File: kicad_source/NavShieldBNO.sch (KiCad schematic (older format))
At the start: 40 parts, among them CN1 ARDUINO_MKR, CN2 CONN_01X04, CN3 CONN_01X04, U1 BNO085, U2 BMP388

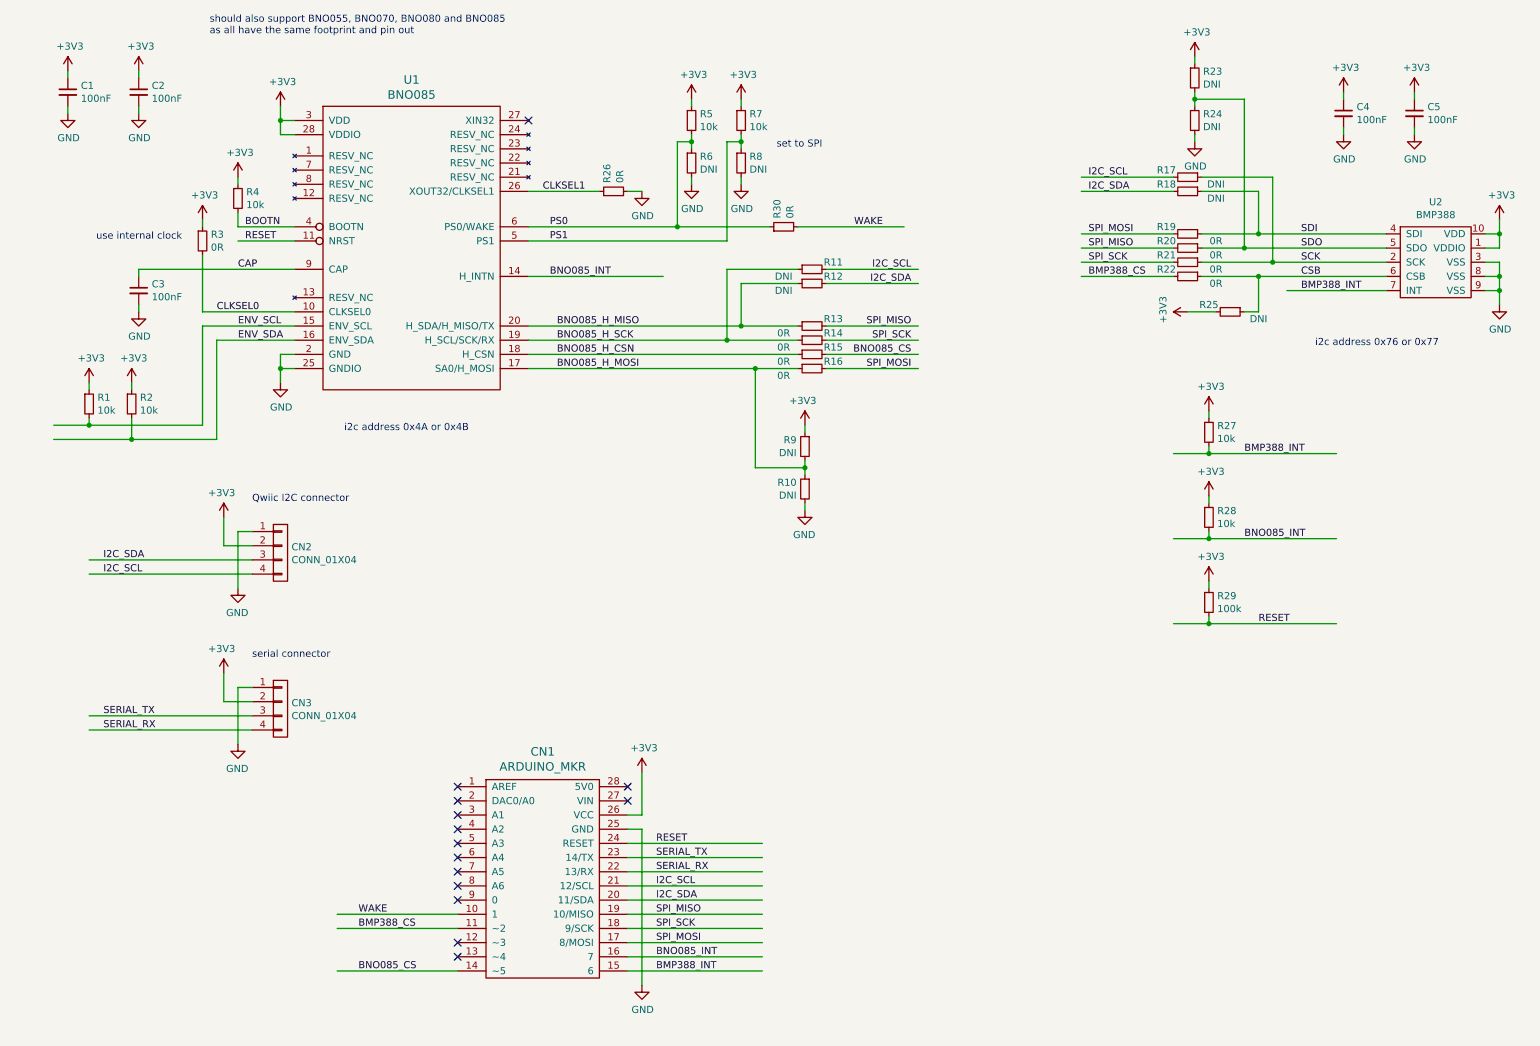
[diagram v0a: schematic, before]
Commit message: added second option for wake on A5, rearranged placement of option resistors and added description in silk screen
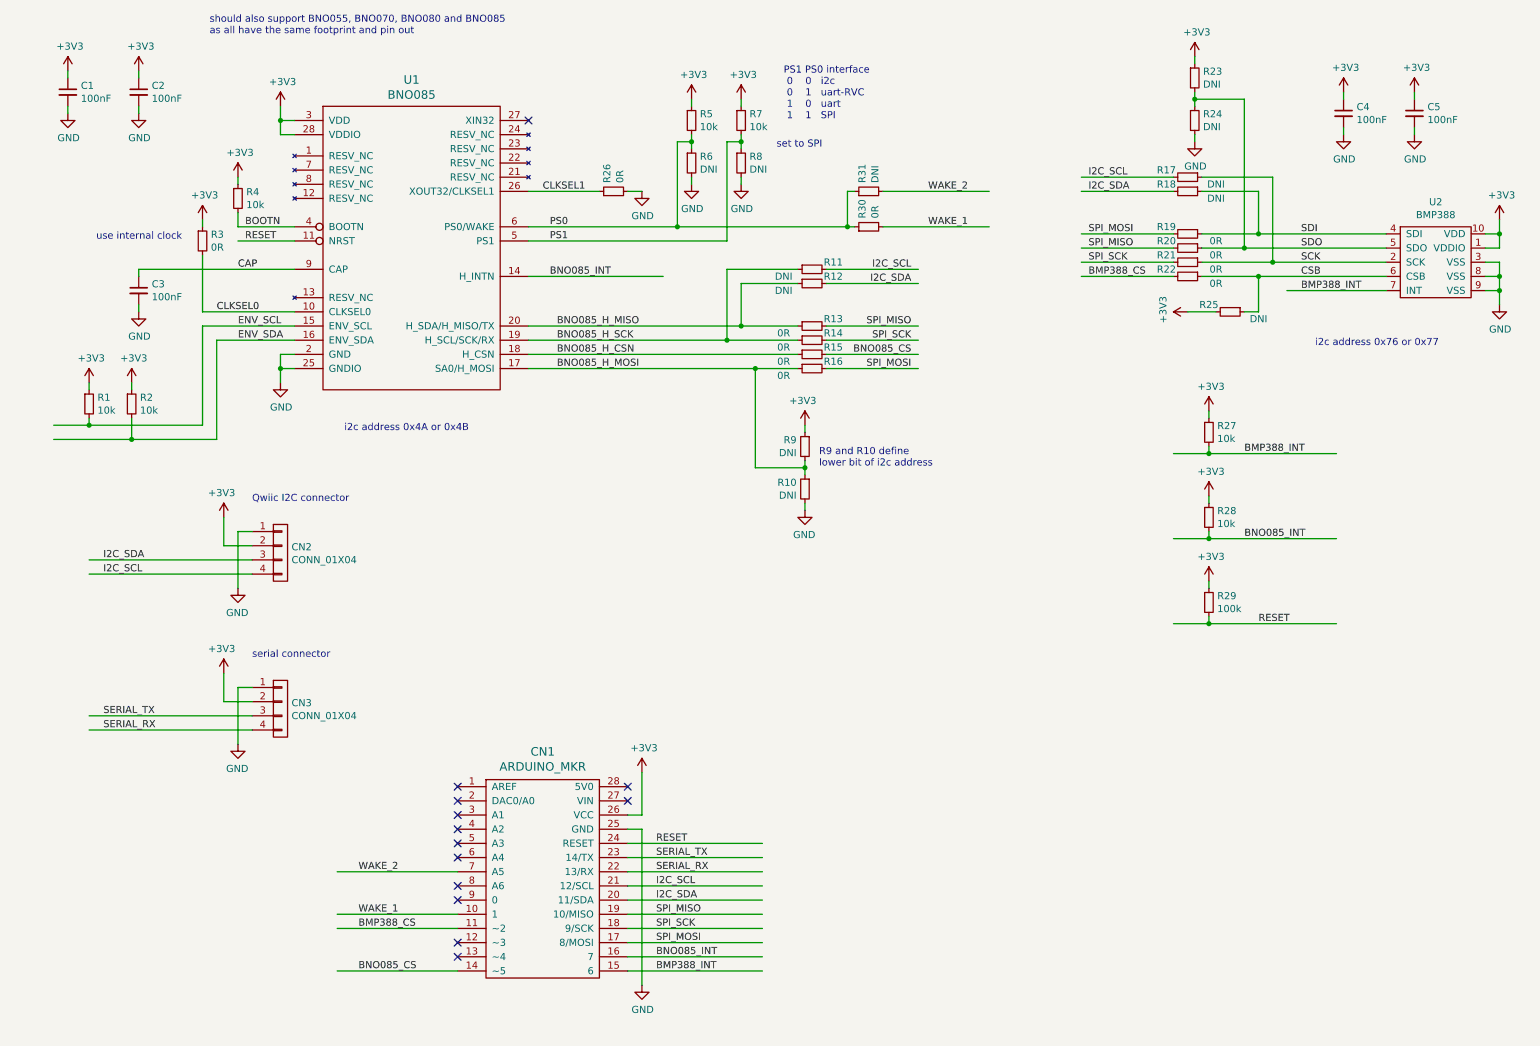
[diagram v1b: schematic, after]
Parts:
- added R31: DNI, resistors:R_0603, symbol devices:R_0603
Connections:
- net labels added: WAKE_1, WAKE_2
- net labels removed: WAKE
- wire segments 159 -> 164
- no-connect marks 14 -> 13
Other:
- note added: "PS1 PS0 interface\n 0 0 i2c\n 0 1 uart-RVC\n 1 0 uart\n 1 1 SPI\n"
- note added: "R9 and R10 define \nlower bit of i2c address"
- moved on the sheet: R30
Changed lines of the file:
@@
 Sheet 1 1
 Title "NavShieldBNO"
-Date "2020-09-17"
+Date "2020-09-25"
 Rev "dev_0.1"
 Comp "generationmake"
@@
 NoConn ~ 3650 6800
 NoConn ~ 3650 6700
-NoConn ~ 3650 6600
 NoConn ~ 3650 6500
 NoConn ~ 3650 6400
@@
 L devices:R_0603 R30
 U 1 1 5F6453B8
-P 5950 2050
-F 0 "R30" H 6009 2096 50  0000 L CNN
-F 1 "0R" H 6009 2005 50  0000 L CNN
-F 2 "resistors:R_0603" H 5950 1900 50  0001 C CNN
-F 3 "" H 5950 2050 50  0000 C CNN
-	1    5950 2050
+P 6550 2050
+F 0 "R30" H 6609 2096 50  0000 L CNN
+F 1 "0R" H 6609 2005 50  0000 L CNN
+F 2 "resistors:R_0603" H 6550 1900 50  0001 C CNN
+F 3 "" H 6550 2050 50  0000 C CNN
+	1    6550 2050
 	0    -1   -1   0
 $EndComp
 Wire Wire Line
-	6800 2050 6050 2050
-Wire Wire Line
-	5850 2050 5200 2050
-Connection ~ 5200 2050
-Text Label 6650 2050 2    50   ~ 0
-WAKE
+	7400 2050 6650 2050
+Wire Wire Line
+	6450 2050 6400 2050
+Text Label 7250 2050 2    50   ~ 0
+WAKE_1
 Wire Wire Line
 	2800 6900 3650 6900
 Text Label 2950 6900 0    50   ~ 0
-WAKE
+WAKE_1
 $Comp
 L mechanical-connectors:CONN_01X04 CN2
@@
 Text Label 4350 2750 0    50   ~ 0
 BNO085_H_MISO
+$Comp
+L devices:R_0603 R31
+U 1 1 5F6DCF1C
+P 6550 1800
+F 0 "R31" H 6609 1846 50  0000 L CNN
+F 1 "DNI" H 6609 1755 50  0000 L CNN
+F 2 "resistors:R_0603" H 6550 1650 50  0001 C CNN
+F 3 "" H 6550 1800 50  0000 C CNN
+	1    6550 1800
+	0    -1   -1   0
+$EndComp
+Text Label 7250 1800 2    50   ~ 0
+WAKE_2
+Wire Wire Line
+	7400 1800 6650 1800
+Wire Wire Line
+	6450 1800 6400 1800
+Wire Wire Line
+	6400 1800 6400 2050
+Connection ~ 6400 2050
+Wire Wire Line
+	2800 6600 3650 6600
+Text Label 2950 6600 0    50   ~ 0
+WAKE_2
+Wire Wire Line
+	5200 2050 6400 2050
+Connection ~ 5200 2050
+Text Notes 6200 3750 0    50   ~ 0
+R9 and R10 define \nlower bit of i2c address
+Text Notes 5950 1300 0    50   ~ 0
+PS1 PS0 interface\n 0    0   i2c\n 0    1   uart-RVC\n 1    0   uart\n 1    1   SPI\n
 $EndSCHEMATC

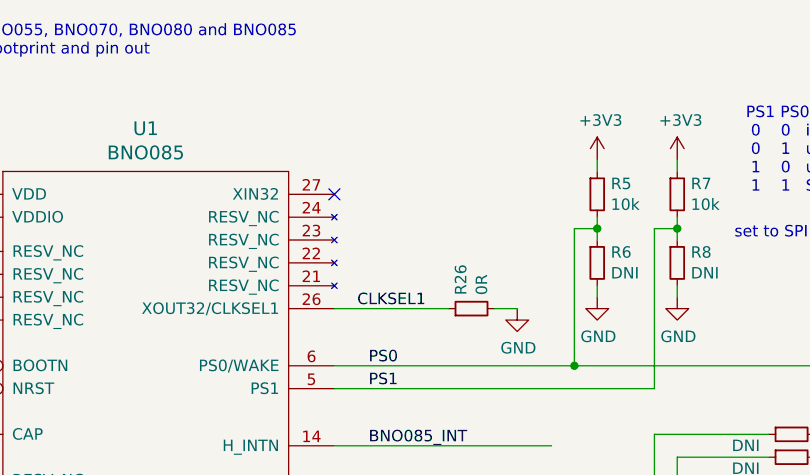
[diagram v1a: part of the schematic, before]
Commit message: added option for 32 kHz crystal, updated images and pdf
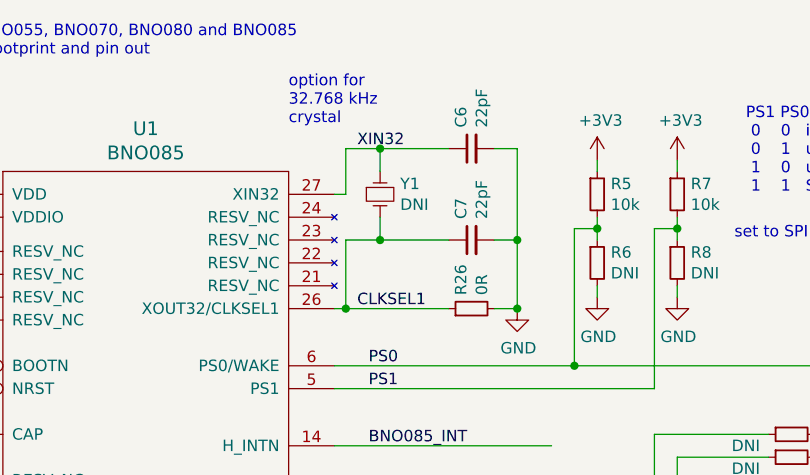
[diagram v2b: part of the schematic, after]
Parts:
- added C6, C7: 22pF, capacitors:C_0603, symbol devices:C_0603
- added Y1: DNI, crystals:Crystal_SMD_3.2x1.5mm_2Pad, symbol devices:Crystal_Small
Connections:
- net labels added: XIN32
- wire segments 164 -> 178
- no-connect marks 13 -> 12
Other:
- note added: "option for\n32.768 kHz\ncrystal"
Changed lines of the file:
@@
 Text Label 2950 7300 0    50   ~ 0
 BNO085_CS
-NoConn ~ 4150 1300
 Wire Wire Line
 	1400 2350 2500 2350
@@
 $EndComp
 Wire Wire Line
-	4150 1800 4650 1800
+	4150 1800 4200 1800
 Wire Wire Line
 	4850 1800 4950 1800
@@
 Text Notes 5950 1300 0    50   ~ 0
 PS1 PS0 interface\n 0    0   i2c\n 0    1   uart-RVC\n 1    0   uart\n 1    1   SPI\n
+$Comp
+L devices:Crystal_Small Y1
+U 1 1 5F6DCF85
+P 4350 1300
+F 0 "Y1" V 4304 1388 50  0000 L CNN
+F 1 "DNI" V 4395 1388 50  0000 L CNN
+F 2 "crystals:Crystal_SMD_3.2x1.5mm_2Pad" V 4441 1388 50  0001 L CNN
+F 3 "" H 4350 1300 50  0000 C CNN
+	1    4350 1300
+	0    1    1    0
+$EndComp
+$Comp
+L devices:C_0603 C7
+U 1 1 5F6DD8D6
+P 4750 1500
+F 0 "C7" H 4842 1546 50  0000 L CNN
+F 1 "22pF" H 4842 1455 50  0000 L CNN
+F 2 "capacitors:C_0603" H 4750 1350 50  0001 C CNN
+F 3 "" H 4750 1500 50  0000 C CNN
+	1    4750 1500
+	0    -1   -1   0
+$EndComp
+$Comp
+L devices:C_0603 C6
+U 1 1 5F6E3776
+P 4750 1100
+F 0 "C6" H 4842 1146 50  0000 L CNN
+F 1 "22pF" H 4842 1055 50  0000 L CNN
+F 2 "capacitors:C_0603" H 4750 950 50  0001 C CNN
+F 3 "" H 4750 1100 50  0000 C CNN
+	1    4750 1100
+	0    -1   -1   0
+$EndComp
+Wire Wire Line
+	4150 1300 4200 1300
+Wire Wire Line
+	4200 1300 4200 1100
+Wire Wire Line
+	4200 1100 4350 1100
+Wire Wire Line
+	4850 1100 4950 1100
+Wire Wire Line
+	4950 1100 4950 1500
+Connection ~ 4950 1800
+Wire Wire Line
+	4650 1500 4350 1500
+Wire Wire Line
+	4200 1500 4200 1800
+Connection ~ 4200 1800
+Wire Wire Line
+	4200 1800 4650 1800
+Wire Wire Line
+	4350 1400 4350 1500
+Connection ~ 4350 1500
+Wire Wire Line
+	4350 1500 4200 1500
+Wire Wire Line
+	4350 1200 4350 1100
+Connection ~ 4350 1100
+Wire Wire Line
+	4350 1100 4650 1100
+Wire Wire Line
+	4850 1500 4950 1500
+Connection ~ 4950 1500
+Wire Wire Line
+	4950 1500 4950 1800
+Text Label 4250 1100 0    50   ~ 0
+XIN32
+Text Notes 3950 1000 0    50   ~ 0
+option for\n32.768 kHz\ncrystal
 $EndSCHEMATC

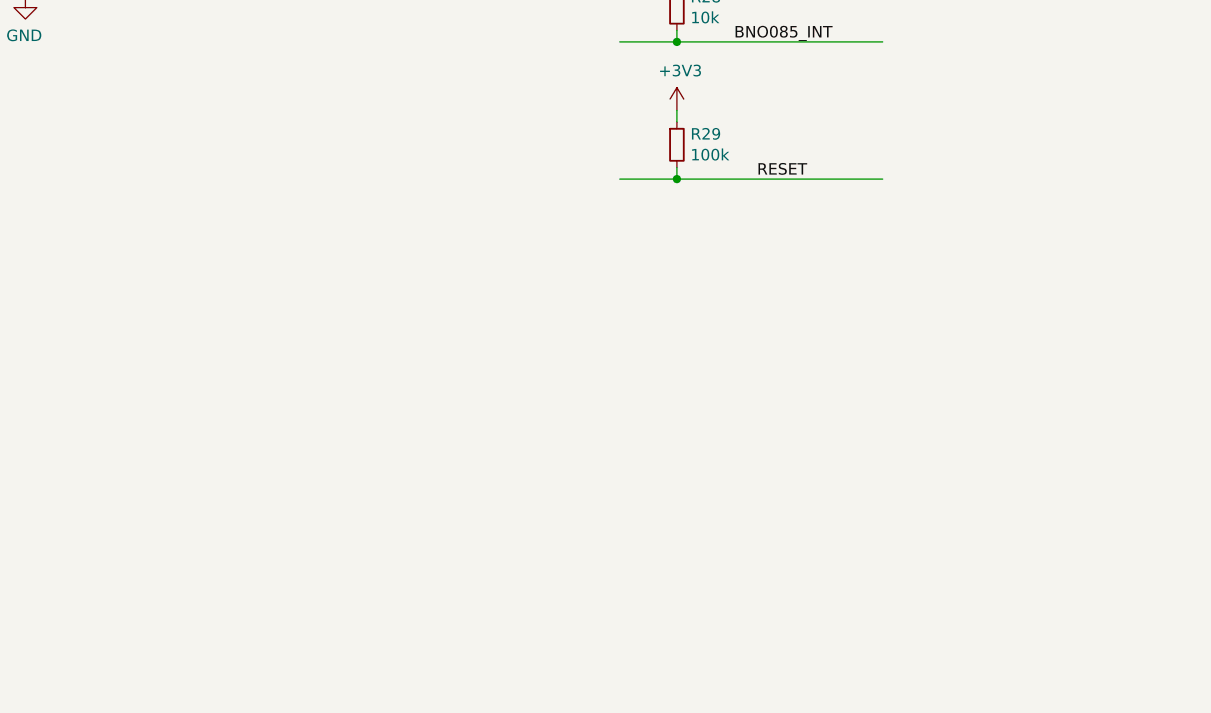
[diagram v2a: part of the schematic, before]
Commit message: added BME280/BMP280
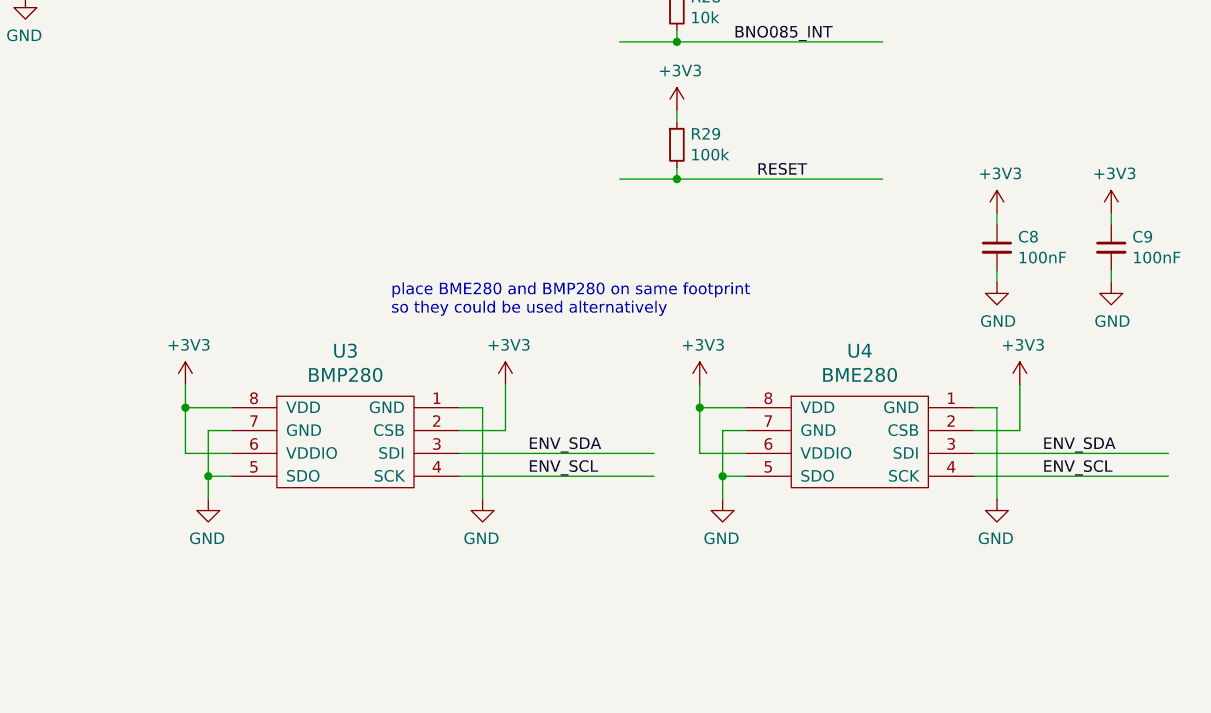
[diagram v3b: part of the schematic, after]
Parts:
- added C8, C9: 100nF, capacitors:C_0603, symbol devices:C_0603
- added U3: BMP280, IC_sensor:BMP280, symbol IC_sensor:BME680
- added U4: BME280, IC_sensor:BME280, symbol IC_sensor:BME680
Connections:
- wire segments 178 -> 210
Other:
- note added: "place BME280 and BMP280 on same footprint\nso they could be used alternatively"
